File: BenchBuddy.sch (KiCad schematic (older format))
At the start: 0 parts

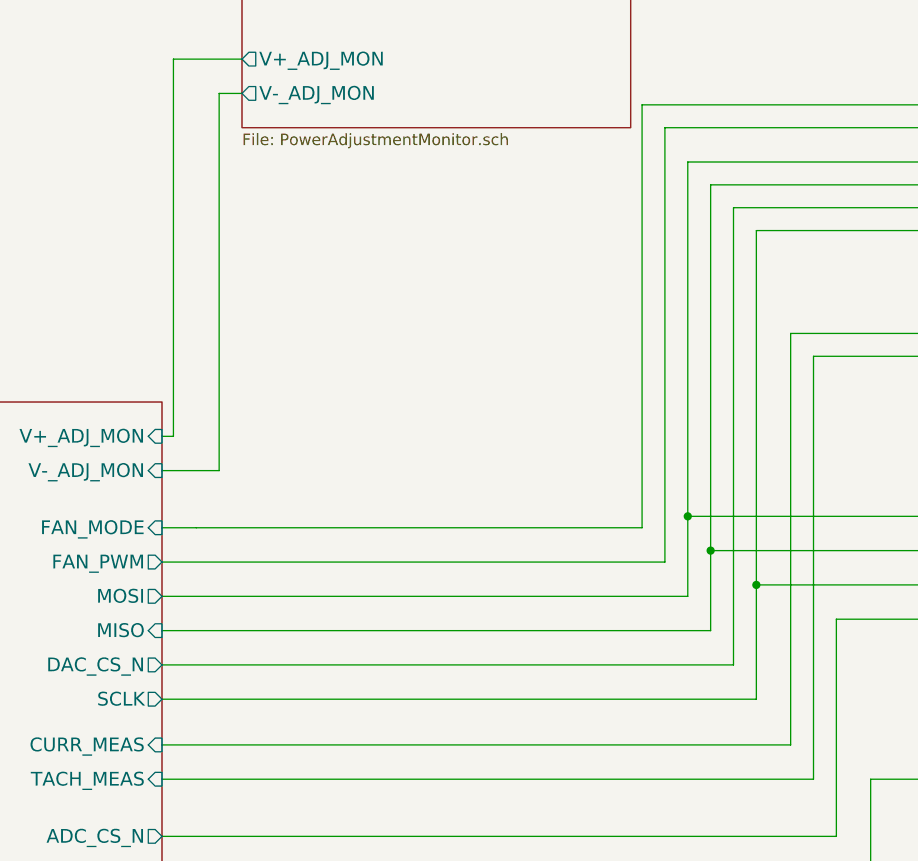
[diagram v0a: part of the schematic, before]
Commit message: Created Footprints and Placed Relay Module
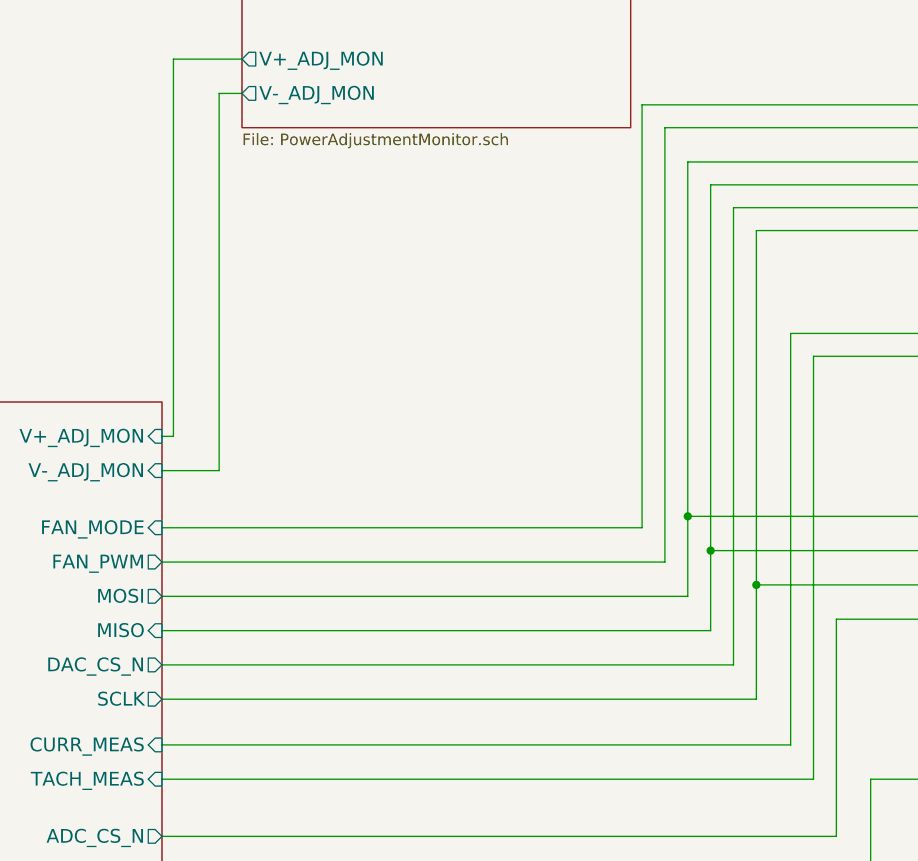
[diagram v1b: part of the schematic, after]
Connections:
- wire segments 58 -> 53
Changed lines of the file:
@@
-EESchema Schematic File Version 2  date 10/10/2013 12:18:22 AM
+EESchema Schematic File Version 2  date 10/10/2013 1:06:29 AM
 LIBS:power
 LIBS:device
@@
 	7750 2350 6700 2350
 Wire Wire Line
-	6700 2350 6700 3900
-Wire Wire Line
-	6700 3900 6700 4250
+	6700 2350 6700 4250
 Wire Wire Line
 	6700 4250 4400 4250
@@
 	7750 2450 6800 2450
 Wire Wire Line
-	6800 2450 6800 4050
-Wire Wire Line
-	6800 4050 6800 4400
+	6800 2450 6800 4400
 Wire Wire Line
 	6800 4400 4400 4400
@@
 	6900 2550 6900 4550
 Wire Wire Line
-	7000 2650 7000 4200
-Wire Wire Line
-	7000 4200 7000 4700
+	7000 2650 7000 4700
 Wire Wire Line
 	7000 4700 4400 4700
@@
 	6500 3950 6500 2100
 Wire Wire Line
-	4550 3950 6500 3950
-Wire Wire Line
-	4550 3950 4550 3950
-Wire Wire Line
-	4550 3950 4400 3950
+	4400 3950 6500 3950
 $EndSCHEMATC

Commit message: Associating Thermocouple Module Components
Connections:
- wire segments 53 -> 59
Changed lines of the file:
@@
-EESchema Schematic File Version 2  date 10/10/2013 1:06:29 AM
+EESchema Schematic File Version 2  date 10/11/2013 1:04:35 AM
 LIBS:power
 LIBS:device
@@
 Sheet 1 9
 Title "noname.sch"
-Date "10 oct 2013"
+Date "11 oct 2013"
 Rev ""
 Comp ""
@@
 $EndDescr
 $Sheet
-S 7800 3700 1700 800
+S 7800 3700 1700 1050
 U 522FEABA
 F0 "Thermocouple" 50
@@
 F5 "MISO" O L 7800 4050 60
 F6 "SCLK" I L 7800 4200 60
-F7 "CS_N" I L 7800 4350 60
-$EndSheet
-$Sheet
-S 750  950  1800 1300
+F7 "~CS" I L 7800 4350 60
+F8 "~RESET" I L 7800 4500 60
+F9 "~DR" O L 7800 4650 60
+$EndSheet
+$Sheet
+S 600  600  1800 1300
 U 522FEADB
 F0 "Power" 50
 F1 "Power.sch" 50
 $EndSheet
+$Sheet
+S 7750 4950 1750 700
+U 522FEB12
+F0 "LED_Driver" 50
+F1 "LED_Driver.sch" 50
+F2 "LED_EN_PWM" I L 7750 5150 60
+F3 "LED_STRING+" O R 9500 5100 60
+F4 "LED_STRING-" O R 9500 5250 60
+$EndSheet
+$Sheet
+S 7750 5900 1750 700
+U 522FEAC6
+F0 "Relay" 50
+F1 "Relay.sch" 50
+F2 "RELAY_NC" B R 9500 6250 60
+F3 "RELAY_NO" B R 9500 6400 60
+F4 "RELAY_COM" B R 9500 6100 60
+F5 "RELAY+" I L 7750 6100 60
+F6 "RELAY-" O L 7750 6250 60
+$EndSheet
+$Sheet
+S 2750 900  1650 900
+U 523DF54E
+F0 "PowerAdjustmentMonitor" 50
+F1 "PowerAdjustmentMonitor.sch" 50
+F2 "V+_ADJ" O R 4400 1100 60
+F3 "V-_ADJ" O R 4400 1300 60
+F4 "3V3_MON" O L 2750 1200 60
+F5 "5V_MON" O L 2750 1000 60
+F6 "V+_ADJ_MON" O L 2750 1500 60
+F7 "V-_ADJ_MON" O L 2750 1650 60
+$EndSheet
+Wire Wire Line
+	10150 1100 4450 1100
+Wire Wire Line
+	4450 1300 10150 1300
+Wire Wire Line
+	9500 2150 10150 2150
+Wire Wire Line
+	10150 2300 9500 2300
+Wire Wire Line
+	9500 3050 10150 3050
+Wire Wire Line
+	9500 6000 10150 6000
+Wire Wire Line
+	10150 6150 9500 6150
+Wire Wire Line
+	9500 6300 10150 6300
+Wire Wire Line
+	2400 3550 2550 3550
+Wire Wire Line
+	2550 3550 2550 1500
+Wire Wire Line
+	2550 1500 2750 1500
+Wire Wire Line
+	2400 3700 2650 3700
+Wire Wire Line
+	2650 3700 2650 1650
+Wire Wire Line
+	2650 1650 2750 1650
+Wire Wire Line
+	2400 4100 4600 4100
+Wire Wire Line
+	4600 4100 4600 2200
+Wire Wire Line
+	4600 2200 7750 2200
+Wire Wire Line
+	7750 2350 4700 2350
+Wire Wire Line
+	4700 2350 4700 4250
+Wire Wire Line
+	4700 4250 2400 4250
+Wire Wire Line
+	7750 2450 4800 2450
+Wire Wire Line
+	4800 2450 4800 4400
+Wire Wire Line
+	4800 4400 2400 4400
+Wire Wire Line
+	7750 2550 4900 2550
+Wire Wire Line
+	4900 2550 4900 4550
+Wire Wire Line
+	5000 2650 5000 4700
+Wire Wire Line
+	5000 4700 2400 4700
+Wire Wire Line
+	7750 3100 5150 3100
+Wire Wire Line
+	5150 3100 5150 4900
+Wire Wire Line
+	5150 4900 2400 4900
+Wire Wire Line
+	7750 3200 5250 3200
+Wire Wire Line
+	5250 3200 5250 5050
+Wire Wire Line
+	5250 5050 2400 5050
+Wire Wire Line
+	7800 3900 4700 3900
+Connection ~ 4700 3900
+Wire Wire Line
+	7800 4050 4800 4050
+Connection ~ 4800 4050
+Wire Wire Line
+	4900 4550 2400 4550
+Wire Wire Line
+	7800 4350 5350 4350
+Wire Wire Line
+	5350 4350 5350 5300
+Wire Wire Line
+	5350 5300 2400 5300
+Wire Wire Line
+	2400 5800 7100 5800
+Wire Wire Line
+	7100 5800 7100 5150
+Wire Wire Line
+	7100 5150 7750 5150
+Wire Wire Line
+	7750 6100 2400 6100
+Wire Wire Line
+	2400 6250 7750 6250
+Wire Wire Line
+	10150 3900 9500 3900
+Wire Wire Line
+	10150 4050 9500 4050
+Wire Wire Line
+	7750 2650 5000 2650
+Wire Wire Line
+	7800 4200 5000 4200
+Connection ~ 5000 4200
+$Sheet
+S 800  3400 1600 3150
+U 522FEA6C
+F0 "Arduino" 50
+F1 "Arduino.sch" 50
+F2 "MOSI" O R 2400 4250 60
+F3 "MISO" I R 2400 4400 60
+F4 "SCLK" O R 2400 4700 60
+F5 "TACH_MEAS" I R 2400 5050 60
+F6 "RELAY+" O R 2400 6100 60
+F7 "RELAY-" O R 2400 6250 60
+F8 "CURR_MEAS" I R 2400 4900 60
+F9 "V+_ADJ_MON" I R 2400 3550 60
+F10 "V-_ADJ_MON" I R 2400 3700 60
+F11 "LED_EN_PWM" O R 2400 5800 60
+F12 "DAC_CS_N" O R 2400 4550 60
+F13 "ADC_CS_N" O R 2400 5300 60
+F14 "FAN_PWM" O R 2400 4100 60
+F15 "FAN_MODE" I R 2400 3950 60
+F16 "~RESET" O R 2400 5450 60
+F17 "~DR" O R 2400 5600 60
+$EndSheet
+Wire Wire Line
+	7750 2100 4500 2100
+Wire Wire Line
+	4500 2100 4500 3950
+Wire Wire Line
+	4500 3950 2400 3950
 $Sheet
 S 7750 1950 1750 1350
@@
 $EndSheet
 $Sheet
-S 7750 4850 1750 700
-U 522FEB12
-F0 "LED_Driver" 50
-F1 "LED_Driver.sch" 50
-F2 "LED_EN_PWM" I L 7750 5050 60
-F3 "LED_STRING+" O R 9500 5000 60
-F4 "LED_STRING-" O R 9500 5150 60
-$EndSheet
-$Sheet
-S 7750 5900 1750 700
-U 522FEAC6
-F0 "Relay" 50
-F1 "Relay.sch" 50
-F2 "RELAY_NC" B R 9500 6250 60
-F3 "RELAY_NO" B R 9500 6400 60
-F4 "RELAY_COM" B R 9500 6100 60
-F5 "RELAY+" I L 7750 6100 60
-F6 "RELAY-" O L 7750 6250 60
-$EndSheet
-$Sheet
-S 4750 900  1700 1300
-U 523DF54E
-F0 "PowerAdjustmentMonitor" 50
-F1 "PowerAdjustmentMonitor.sch" 50
-F2 "V+_ADJ" O R 6450 1100 60
-F3 "V-_ADJ" O R 6450 1300 60
-F4 "3V3_MON" O L 4750 1200 60
-F5 "5V_MON" O L 4750 1000 60
-F6 "V+_ADJ_MON" O L 4750 1900 60
-F7 "V-_ADJ_MON" O L 4750 2050 60
-$EndSheet
-$Sheet
 S 10150 850  750  5700
 U 522FEB54
@@
 F5 "FAN_OUT-" O L 10150 2300 60
 F6 "TACH_IN" I L 10150 3050 60
-F7 "LED_STRING+" O L 10150 5000 60
-F8 "LED_STRING-" O L 10150 5150 60
+F7 "LED_STRING+" O L 10150 5100 60
+F8 "LED_STRING-" O L 10150 5250 60
 F9 "TC_IN+" I L 10150 3900 60
 F10 "TC_IN-" I L 10150 4050 60
@@
 $EndSheet
 Wire Wire Line
-	10150 1100 6450 1100
-Wire Wire Line
-	6450 1300 10150 1300
-Wire Wire Line
-	9500 2150 10150 2150
-Wire Wire Line
-	10150 2300 9500 2300
-Wire Wire Line
-	9500 3050 10150 3050
-Wire Wire Line
-	9500 6000 10150 6000
-Wire Wire Line
-	10150 6150 9500 6150
-Wire Wire Line
-	9500 6300 10150 6300
-Wire Wire Line
-	4400 3550 4450 3550
-Wire Wire Line
-	4450 3550 4450 1900
-Wire Wire Line
-	4450 1900 4750 1900
-Wire Wire Line
-	4400 3700 4650 3700
-Wire Wire Line
-	4650 3700 4650 2050
-Wire Wire Line
-	4650 2050 4750 2050
-Wire Wire Line
-	4400 4100 6600 4100
-Wire Wire Line
-	6600 4100 6600 2200
-Wire Wire Line
-	6600 2200 7750 2200
-Wire Wire Line
-	7750 2350 6700 2350
-Wire Wire Line
-	6700 2350 6700 4250
-Wire Wire Line
-	6700 4250 4400 4250
-Wire Wire Line
-	7750 2450 6800 2450
-Wire Wire Line
-	6800 2450 6800 4400
-Wire Wire Line
-	6800 4400 4400 4400
-Wire Wire Line
-	7750 2550 6900 2550
-Wire Wire Line
-	6900 2550 6900 4550
-Wire Wire Line
-	7000 2650 7000 4700
-Wire Wire Line
-	7000 4700 4400 4700
-Wire Wire Line
-	7750 3100 7150 3100
-Wire Wire Line
-	7150 3100 7150 4900
-Wire Wire Line
-	7150 4900 4400 4900
-Wire Wire Line
-	7750 3200 7250 3200
-Wire Wire Line
-	7250 3200 7250 5050
-Wire Wire Line
-	7250 5050 4400 5050
-Wire Wire Line
-	7800 3900 6700 3900
-Connection ~ 6700 3900
-Wire Wire Line
-	7800 4050 6800 4050
-Connection ~ 6800 4050
-Wire Wire Line
-	6900 4550 4400 4550
-Wire Wire Line
-	7800 4350 7350 4350
-Wire Wire Line
-	7350 4350 7350 5300
-Wire Wire Line
-	7350 5300 4400 5300
-Wire Wire Line
-	4450 5800 7500 5800
-Wire Wire Line
-	7500 5800 7500 5050
-Wire Wire Line
-	7500 5050 7750 5050
-Wire Wire Line
-	7750 6100 4400 6100
-Wire Wire Line
-	4400 6250 7750 6250
-Wire Wire Line
-	10150 3900 9500 3900
-Wire Wire Line
-	10150 4050 9500 4050
-Wire Wire Line
-	10150 5150 9500 5150
-Wire Wire Line
-	9500 5000 10150 5000
-Wire Wire Line
-	7750 2650 7000 2650
-Wire Wire Line
-	7800 4200 7000 4200
-Connection ~ 7000 4200
-$Sheet
-S 2800 3400 1600 3150
-U 522FEA6C
-F0 "Arduino" 50
-F1 "Arduino.sch" 50
-F2 "MOSI" O R 4400 4250 60
-F3 "MISO" I R 4400 4400 60
-F4 "SCLK" O R 4400 4700 60
-F5 "TACH_MEAS" I R 4400 5050 60
-F6 "RELAY+" O R 4400 6100 60
-F7 "RELAY-" O R 4400 6250 60
-F8 "CURR_MEAS" I R 4400 4900 60
-F9 "V+_ADJ_MON" I R 4400 3550 60
-F10 "V-_ADJ_MON" I R 4400 3700 60
-F11 "LED_EN_PWM" O R 4400 5800 60
-F12 "DAC_CS_N" O R 4400 4550 60
-F13 "ADC_CS_N" O R 4400 5300 60
-F14 "FAN_PWM" O R 4400 4100 60
-F15 "FAN_MODE" I R 4400 3950 60
-$EndSheet
-Wire Wire Line
-	7750 2100 6500 2100
-Wire Wire Line
-	6500 3950 6500 2100
-Wire Wire Line
-	4400 3950 6500 3950
+	9500 5100 10150 5100
+Wire Wire Line
+	9550 5250 10150 5250
+Wire Wire Line
+	2400 5450 5500 5450
+Wire Wire Line
+	5500 5450 5500 4500
+Wire Wire Line
+	5500 4500 7800 4500
+Wire Wire Line
+	7800 4650 5650 4650
+Wire Wire Line
+	5650 4650 5650 5600
+Wire Wire Line
+	5650 5600 2400 5600
 $EndSCHEMATC
